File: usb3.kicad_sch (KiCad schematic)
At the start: 50 parts, among them J5 Conn_USB-C_WE_632723300011, Q19 PJE138K, Q4 PJE138K, U17 HD3SS3220RNH, U18 AP22615A_TSOT26, U19 TPD4E05U06QDQARQ1, U20 TPD4E05U06QDQARQ1, U21 TPD4E05U06QDQARQ1

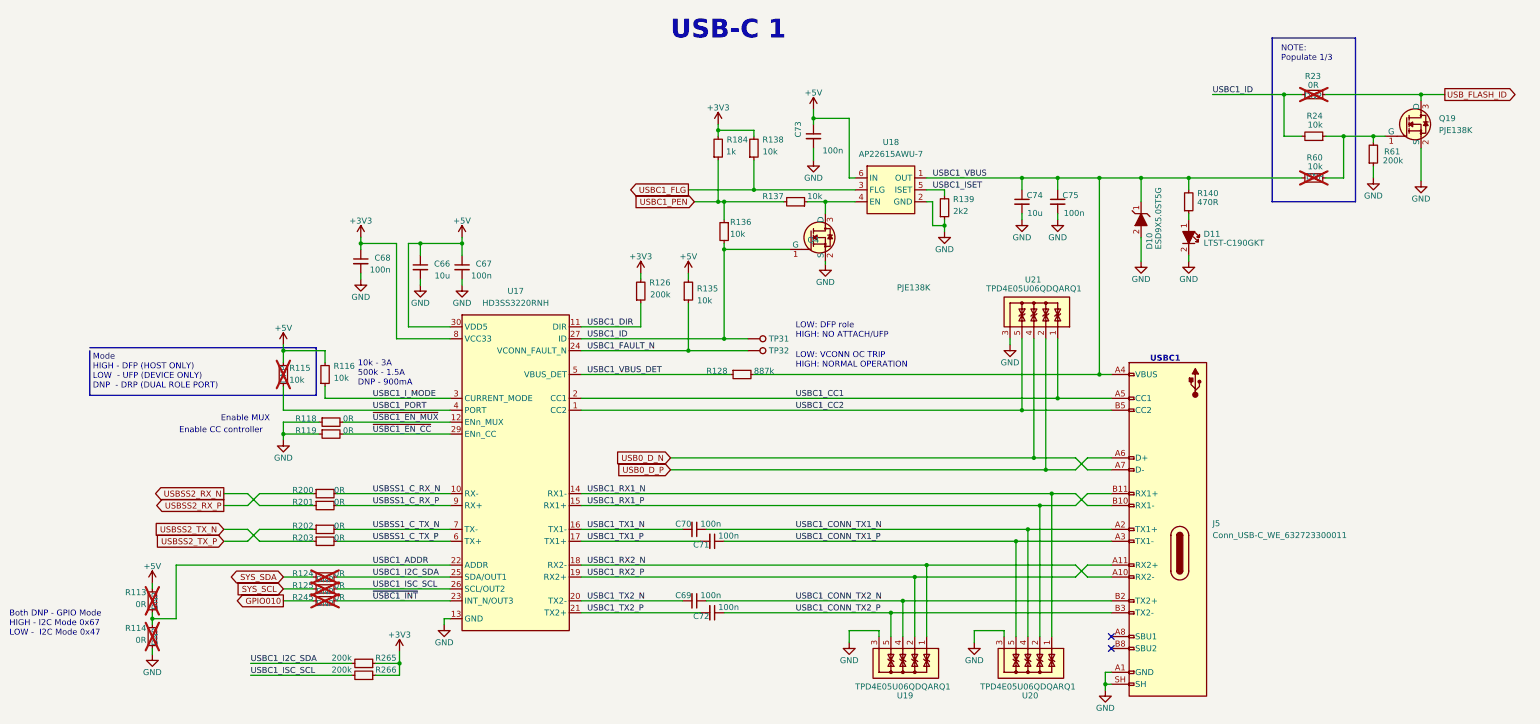
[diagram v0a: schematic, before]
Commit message: 5/16 Commit: Sch Mods added and beginning Development on PCB layout
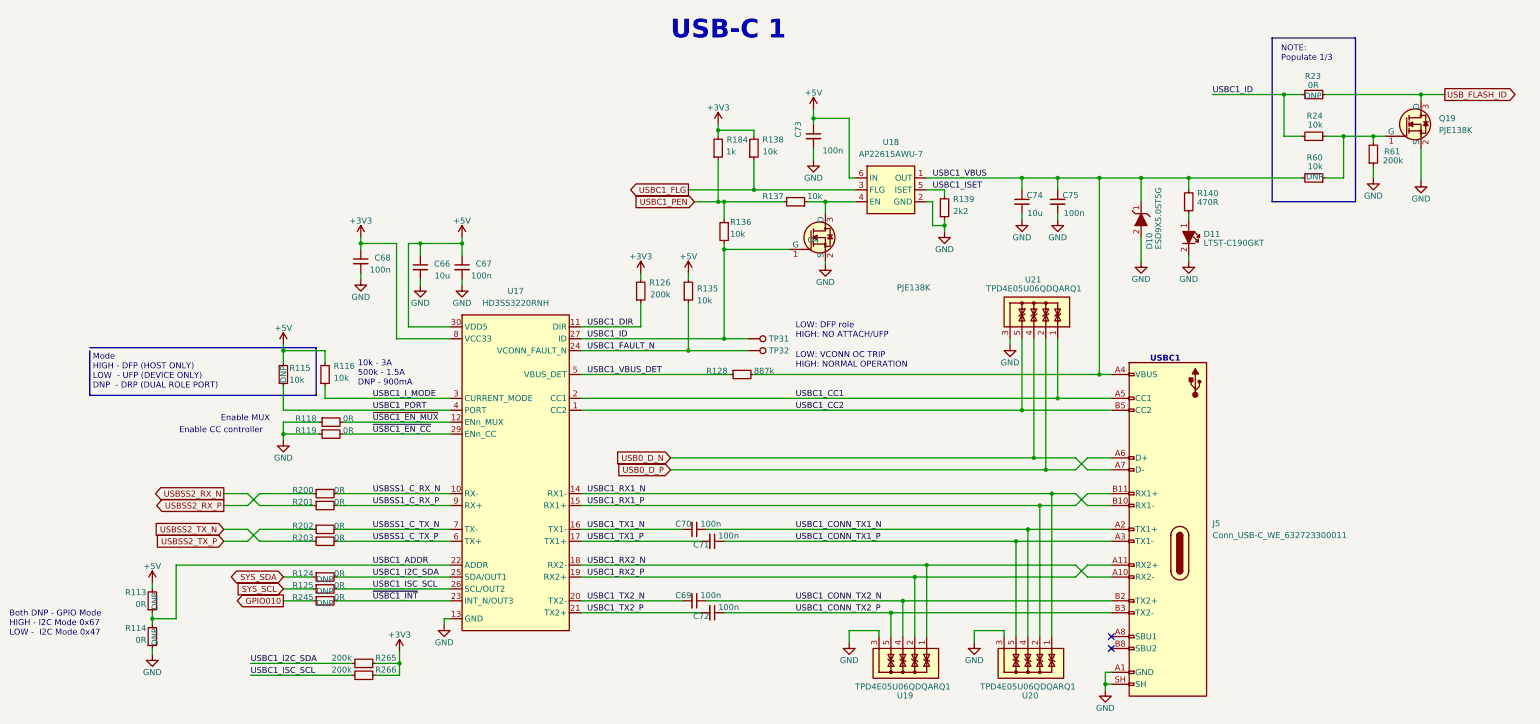
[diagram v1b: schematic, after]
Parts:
- R113, R114, R115, R124, R125, R23, R245, R60: now fitted
